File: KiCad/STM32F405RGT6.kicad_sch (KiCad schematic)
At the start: 52 parts, among them J1 Conn_02x05_Odd_Even, J2 USB_C_Receptacle_USB2.0, SW1 TS-1187A, SW2 TS-1187A, U1 M24C02-RMN, U2 STM32F405RGTx, U3 AMS1117-3.3, U4 SRV05-4, Y1 16MHz

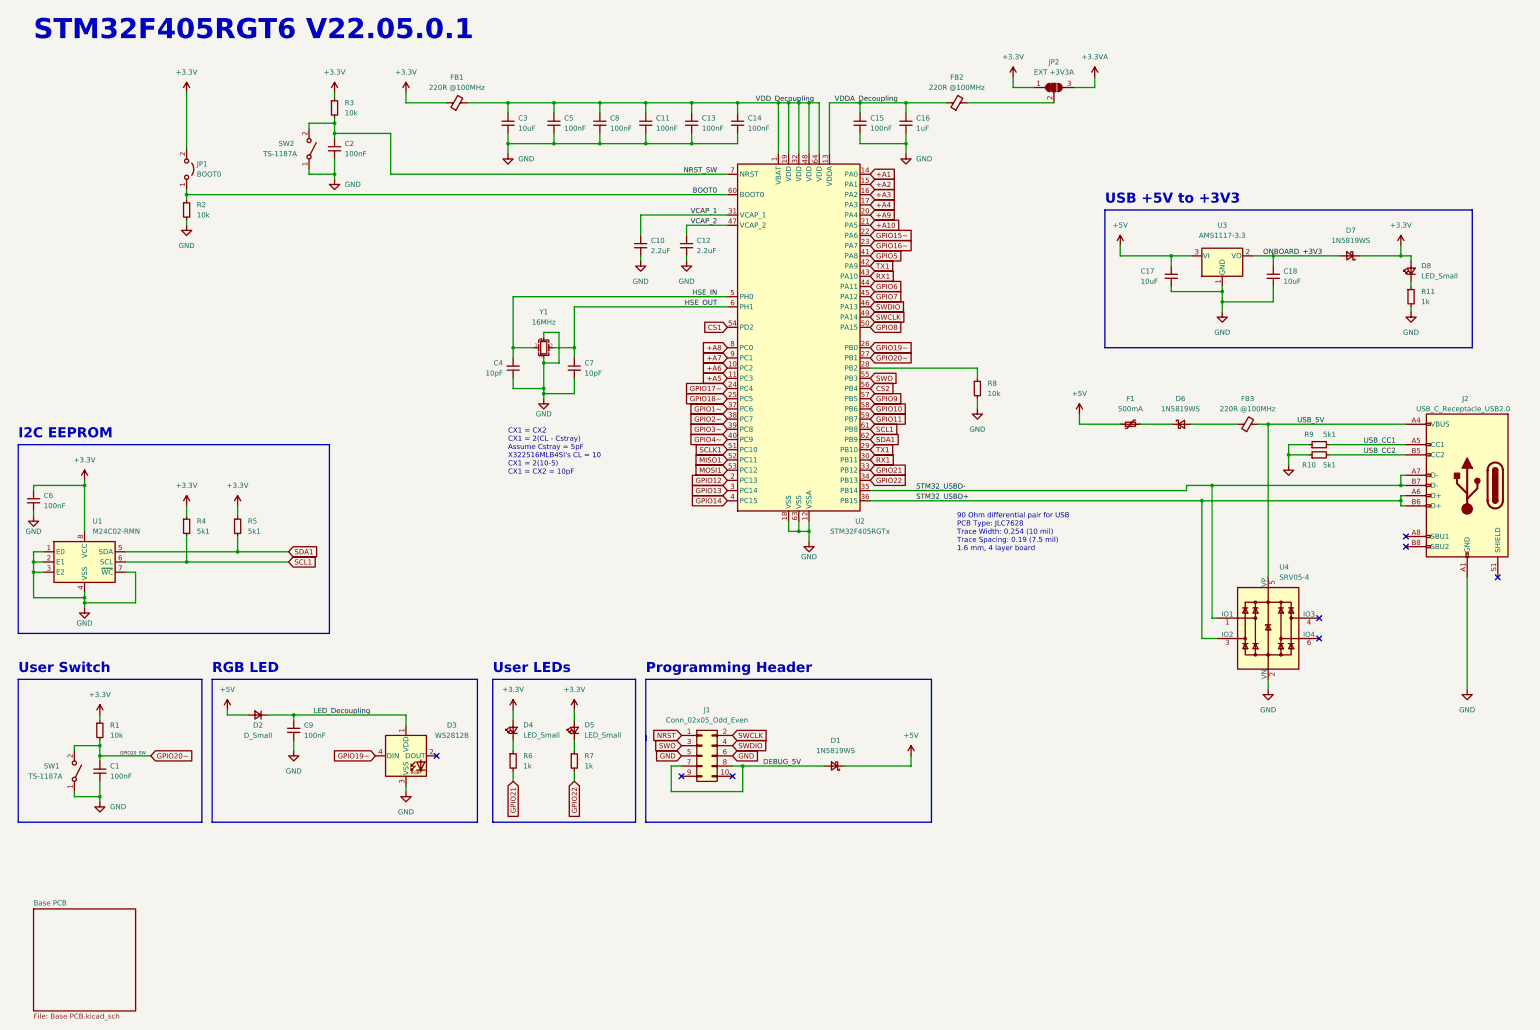
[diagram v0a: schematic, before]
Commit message: Added part numbers to most parts
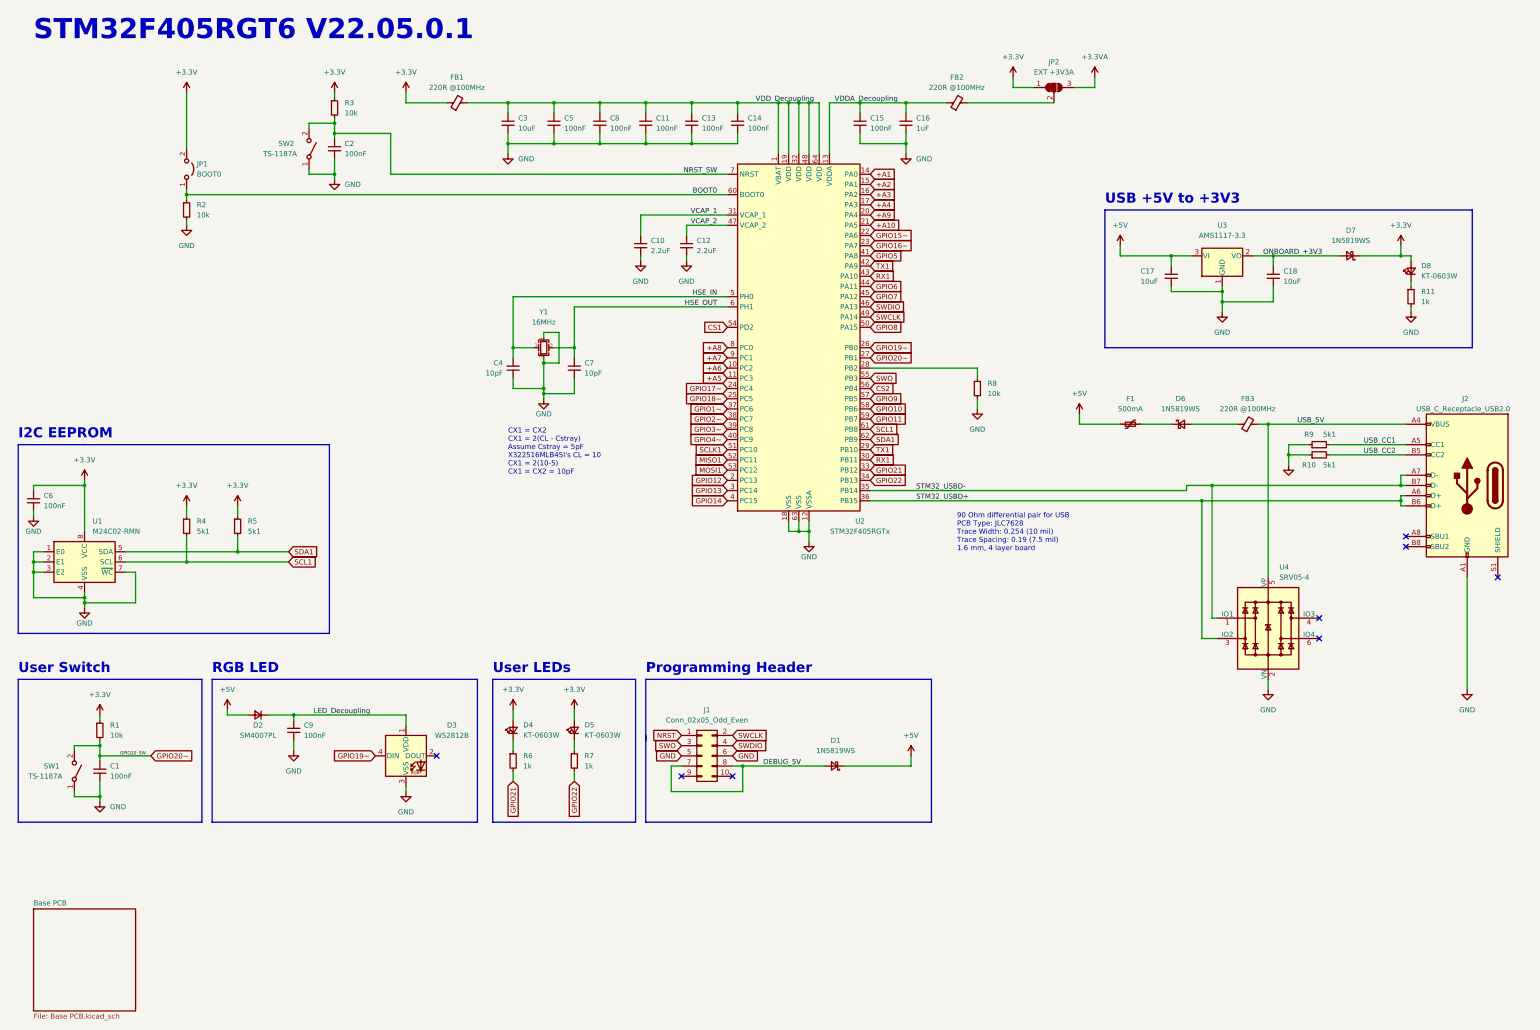
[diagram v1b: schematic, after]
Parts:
- C1, C11, C13, C14, C15, C2, C5, C6, C8, C9: JLCPCB Part # (none) -> C14663; Part Number (none) -> CC0603KRX7R9BB104
- C10, C12: JLCPCB Part # (none) -> C23630; Part Number (none) -> CL10A225KO8NNNC
- C16: JLCPCB Part # (none) -> C15849; Part Number (none) -> CL10A105KB8NNNC
- C17, C18, C3: JLCPCB Part # (none) -> C19702; Part Number (none) -> CL10A106KP8NNNC
- C4, C7: JLCPCB Part # (none) -> C1634; Part Number (none) -> CL10C100JB8NNNC
- D2: value D_Small -> SM4007PL; JLCPCB Part # (none) -> C64898; Part Number (none) -> SM4007PL
- D4, D5, D8: value LED_Small -> KT-0603W; JLCPCB Part # (none) -> C2290
- R1, R2, R3, R8: JLCPCB Part # (none) -> C25804; Part Number (none) -> 0603WAF1002T5E
- R10, R4, R5, R9: JLCPCB Part # (none) -> C23186; Part Number (none) -> 0603WAF5101T5E
- R11, R6, R7: JLCPCB Part # (none) -> C21190; Part Number (none) -> 0603WAF1001T5E
- U2: JLCPCB Part # (none) -> C15742; Part Number (none) -> STM32F405RGT6
- U3: JLCPCB Part # (none) -> C6186; Part Number (none) -> AMS1117-3.3

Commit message: Update Schematic and PCB
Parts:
- removed JP2: EXT +3V3A, Jumper:SolderJumper-3_P1.3mm_Bridged12_RoundedPad1.0x1.5mm, symbol Jumper:SolderJumper_3_Bridged12
- JP1: JLCPCB Part # (none) -> C492401; Part Number (none) -> PZ254V-11-02P
- renumbered C6 to C1, C1 to C2, C9 to C3, C2 to C4, C3 to C5, C4 to C6, C5 to C7, C7 to C8, C8 to C9, D2 to D1, D3 to D2, D4 to D3, D5 to D4, D1 to D5, R4 to R3, R5 to R4, R3 to R5
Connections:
- net +3V3: now also FB2.2
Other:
- moved on the sheet: C10, FB2

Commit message: Started Routing
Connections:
- net NRST_SW is gone; now on net NRST: C4.1, R5.2, SW2.2 (B), U2.7 (NRST)
- net RX1: no longer U2.30 (PB11)
- net TX1: no longer U2.29 (PB10)
- new net RX2: U2.30 (PB11)
- new net TX2: U2.29 (PB10)
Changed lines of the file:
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@@
   (junction (at 166.37 50.8) (diameter 0) (color 0 0 0 0)
+  )
+  (junction (at 93.98 45.72) (diameter 0) (color 0 0 0 0)
   )
   (junction (at 25.4 154.94) (diameter 0) (color 0 0 0 0)
@@
     (stroke (width 0) (type default) (color 0 0 0 0))
   )
+  (wire (pts (xy 93.98 45.72) (xy 100.33 45.72))
+    (stroke (width 0) (type default) (color 0 0 0 0))
+  )
   (wire (pts (xy 365.76 76.2) (xy 365.76 78.74))
     (stroke (width 0) (type default) (color 0 0 0 0))
@@
     (stroke (width 0) (type default) (color 0 0 0 0))
   )
-  (wire (pts (xy 93.98 45.72) (xy 100.33 45.72))
+  (wire (pts (xy 92.71 45.72) (xy 93.98 45.72))
     (stroke (width 0) (type default) (color 0 0 0 0))
   )
@@
     )
   )
-  (global_label "RX1" (shape input) (at 233.68 129.54 0) (fields_autoplaced)
-    (effects (font (size 1.27 1.27)) (justify left))
-    (property "Intersheet References" "${INTERSHEET_REFS}" (id 0) (at 138.43 63.5 0)
-      (effects (font (size 1.27 1.27)) hide)
+  (global_label "RX2" (shape input) (at 233.68 129.54 0) (fields_autoplaced)
+    (effects (font (size 1.27 1.27)) (justify left))
+    (property "Intersheet References" "${INTERSHEET_REFS}" (id 0) (at 239.6932 129.4606 0)
+      (effects (font (size 1.27 1.27)) (justify left) hide)
     )
   )
@@
     )
   )
-  (global_label "TX1" (shape input) (at 233.68 127 0) (fields_autoplaced)
-    (effects (font (size 1.27 1.27)) (justify left))
-    (property "Intersheet References" "${INTERSHEET_REFS}" (id 0) (at 316.23 193.04 0)
-      (effects (font (size 1.27 1.27)) hide)
+  (global_label "TX2" (shape input) (at 233.68 127 0) (fields_autoplaced)
+    (effects (font (size 1.27 1.27)) (justify left))
+    (property "Intersheet References" "${INTERSHEET_REFS}" (id 0) (at 239.3909 126.9206 0)
+      (effects (font (size 1.27 1.27)) (justify left) hide)
     )
   )
@@
     )
   )
+  (global_label "NRST" (shape input) (at 92.71 45.72 180) (fields_autoplaced)
+    (effects (font (size 1.27 1.27)) (justify right))
+    (property "Intersheet References" "${INTERSHEET_REFS}" (id 0) (at 85.6082 45.6406 0)
+      (effects (font (size 1.27 1.27)) (justify right) hide)
+    )
+  )

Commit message: Updated PCB
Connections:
- net STM32_USBD+: now also U4.1 (IO1); no longer U4.3 (IO2)
- net STM32_USBD-: now also U4.6 (IO4); no longer U4.1 (IO1)
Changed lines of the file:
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@@
   (junction (at 321.31 87.63) (diameter 0) (color 0 0 0 0)
   )
-  (junction (at 316.23 139.7) (diameter 0) (color 0 0 0 0)
+  (junction (at 346.71 135.89) (diameter 0) (color 0 0 0 0)
   )
   (junction (at 218.44 147.32) (diameter 0) (color 0 0 0 0)
@@
   (junction (at 41.91 213.36) (diameter 0) (color 0 0 0 0)
   )
+  (junction (at 318.77 139.7) (diameter 0) (color 0 0 0 0)
+  )
   (junction (at 41.91 203.2) (diameter 0) (color 0 0 0 0)
   )
@@
   )
   (junction (at 143.51 50.8) (diameter 0) (color 0 0 0 0)
-  )
-  (junction (at 318.77 135.89) (diameter 0) (color 0 0 0 0)
   )
   (junction (at 118.11 193.04) (diameter 0) (color 0 0 0 0)
@@
   (no_connect (at 186.69 208.28))
   (no_connect (at 199.39 208.28))
-  (no_connect (at 345.44 173.99))
   (no_connect (at 389.89 158.75))
-  (no_connect (at 345.44 168.91))
+  (no_connect (at 320.04 173.99))
   (no_connect (at 367.03 148.59))
   (no_connect (at 367.03 151.13))
+  (no_connect (at 345.44 168.91))
   (wire (pts (xy 350.52 78.74) (xy 334.01 78.74))
     (stroke (width 0) (type default) (color 0 0 0 0))
@@
     (stroke (width 0) (type default) (color 0 0 0 0))
   )
+  (wire (pts (xy 346.71 135.89) (xy 346.71 173.99))
+    (stroke (width 0) (type default) (color 0 0 0 0))
+  )
   (wire (pts (xy 143.51 50.8) (xy 143.51 48.26))
     (stroke (width 0) (type default) (color 0 0 0 0))
@@
     (stroke (width 0) (type default) (color 0 0 0 0))
   )
-  (wire (pts (xy 233.68 139.7) (xy 316.23 139.7))
-    (stroke (width 0) (type default) (color 0 0 0 0))
-  )
   (wire (pts (xy 118.11 38.1) (xy 118.11 40.64))
     (stroke (width 0) (type default) (color 0 0 0 0))
@@
     (stroke (width 0) (type default) (color 0 0 0 0))
   )
+  (wire (pts (xy 318.77 139.7) (xy 318.77 168.91))
+    (stroke (width 0) (type default) (color 0 0 0 0))
+  )
   (polyline (pts (xy 383.54 67.31) (xy 383.54 101.6))
     (stroke (width 0) (type default) (color 0 0 0 0))
@@
     (stroke (width 0) (type default) (color 0 0 0 0))
   )
-  (wire (pts (xy 318.77 168.91) (xy 318.77 135.89))
-    (stroke (width 0) (type default) (color 0 0 0 0))
-  )
   (wire (pts (xy 279.4 40.64) (xy 279.4 38.1))
     (stroke (width 0) (type default) (color 0 0 0 0))
@@
     (stroke (width 0) (type default) (color 0 0 0 0))
   )
+  (wire (pts (xy 346.71 173.99) (xy 345.44 173.99))
+    (stroke (width 0) (type default) (color 0 0 0 0))
+  )
   (wire (pts (xy 154.94 101.6) (xy 160.02 101.6))
     (stroke (width 0) (type default) (color 0 0 0 0))
@@
     (stroke (width 0) (type default) (color 0 0 0 0))
   )
-  (wire (pts (xy 318.77 135.89) (xy 365.76 135.89))
+  (wire (pts (xy 312.42 135.89) (xy 346.71 135.89))
     (stroke (width 0) (type default) (color 0 0 0 0))
   )
@@
     (stroke (width 0) (type default) (color 0 0 0 0))
   )
+  (wire (pts (xy 318.77 139.7) (xy 365.76 139.7))
+    (stroke (width 0) (type default) (color 0 0 0 0))
+  )
   (wire (pts (xy 245.11 40.64) (xy 242.57 40.64))
     (stroke (width 0) (type default) (color 0 0 0 0))
@@
     (stroke (width 0) (type default) (color 0 0 0 0))
   )
-  (wire (pts (xy 312.42 135.89) (xy 318.77 135.89))
-    (stroke (width 0) (type default) (color 0 0 0 0))
-  )
   (wire (pts (xy 332.74 120.65) (xy 367.03 120.65))
     (stroke (width 0) (type default) (color 0 0 0 0))
@@
     (stroke (width 0) (type default) (color 0 0 0 0))
   )
+  (wire (pts (xy 346.71 135.89) (xy 365.76 135.89))
+    (stroke (width 0) (type default) (color 0 0 0 0))
+  )
   (wire (pts (xy 189.23 48.26) (xy 189.23 50.8))
     (stroke (width 0) (type default) (color 0 0 0 0))
@@
     (stroke (width 0) (type default) (color 0 0 0 0))
   )
-  (wire (pts (xy 316.23 173.99) (xy 316.23 139.7))
-    (stroke (width 0) (type default) (color 0 0 0 0))
-  )
   (wire (pts (xy 242.57 50.8) (xy 242.57 53.34))
     (stroke (width 0) (type default) (color 0 0 0 0))
@@
     (stroke (width 0) (type default) (color 0 0 0 0))
   )
-  (wire (pts (xy 320.04 173.99) (xy 316.23 173.99))
-    (stroke (width 0) (type default) (color 0 0 0 0))
-  )
   (wire (pts (xy 262.89 40.64) (xy 279.4 40.64))
     (stroke (width 0) (type default) (color 0 0 0 0))
@@
     (stroke (width 0) (type default) (color 0 0 0 0))
   )
-  (wire (pts (xy 316.23 139.7) (xy 365.76 139.7))
-    (stroke (width 0) (type default) (color 0 0 0 0))
-  )
   (wire (pts (xy 186.69 205.74) (xy 184.15 205.74))
     (stroke (width 0) (type default) (color 0 0 0 0))
@@
     (stroke (width 0) (type default) (color 0 0 0 0))
   )
+  (wire (pts (xy 233.68 139.7) (xy 318.77 139.7))
+    (stroke (width 0) (type default) (color 0 0 0 0))
+  )
